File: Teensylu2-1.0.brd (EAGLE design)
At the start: 101.6 x 76.2 mm, 114 parts, among them J1 M02POLAR, J10 HOTEND-2, J11 M02POLAR, J12 M02POLAR, J13 M02POLAR, J2 MICROSD, J3 USB-MICRO-PTH, J4 M02POLAR, J5 4P-TERM-BLOCK284391-4, J6 39-29-3066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

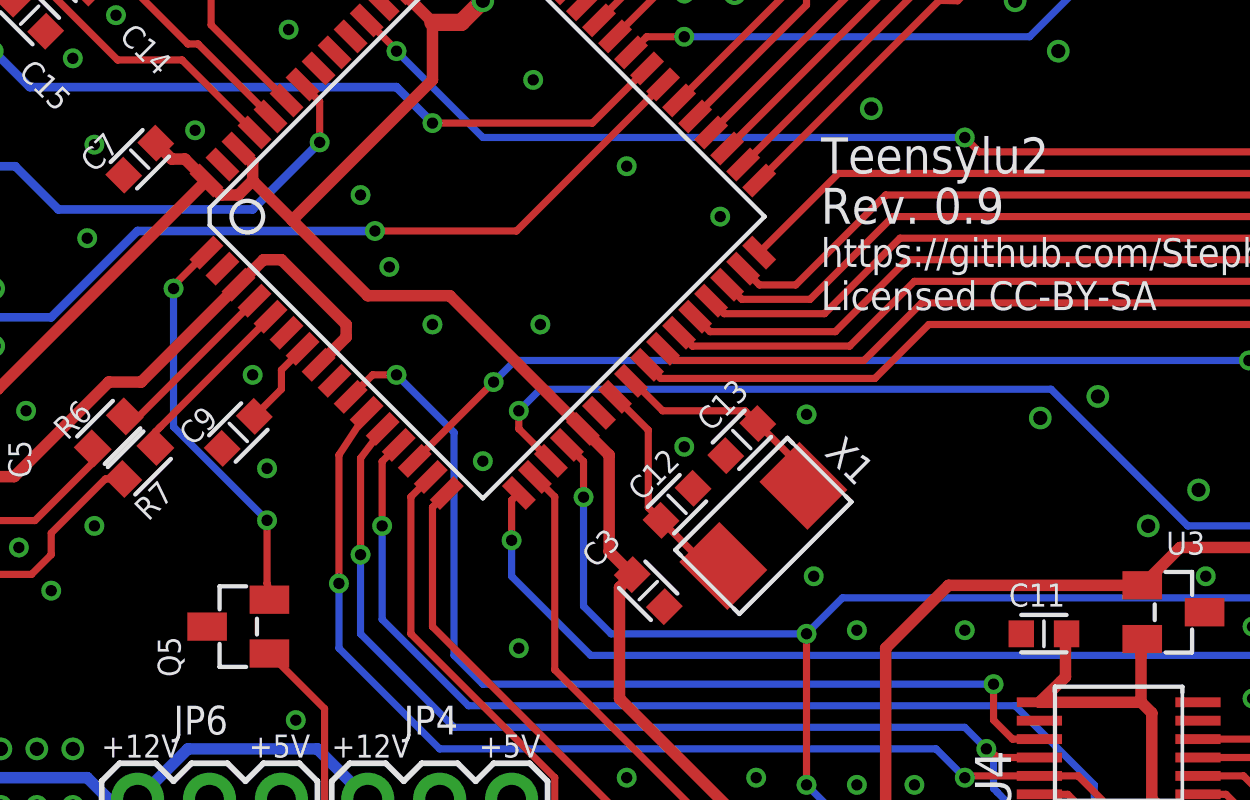
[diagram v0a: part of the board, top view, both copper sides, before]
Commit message: Fixed Z Endstop
Collector and Emitter were swapped.
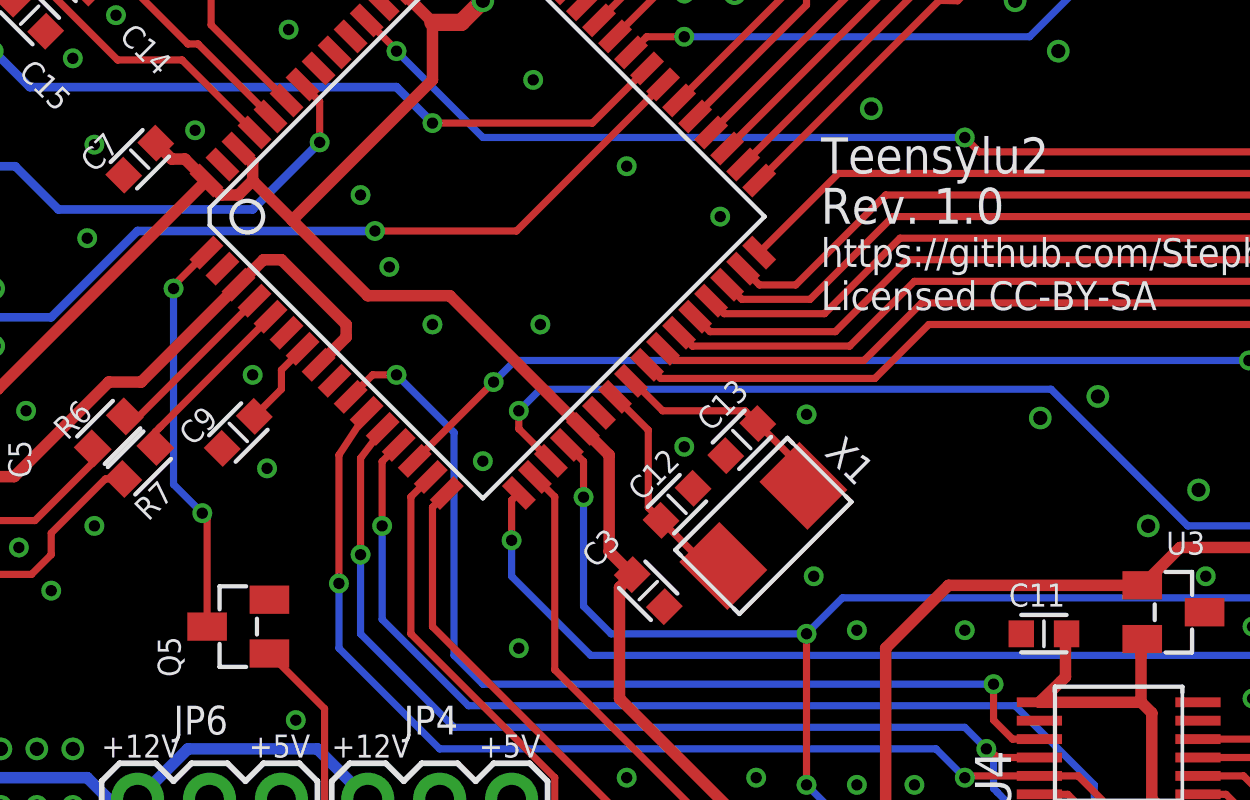
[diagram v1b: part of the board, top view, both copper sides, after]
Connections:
- net GND: now also Q5.2; no longer Q5.3
- net Z-STOP: now also Q5.3; no longer Q5.2
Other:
- board text added: "Rev. 1.0"
- board text removed: "Rev. 0.9"
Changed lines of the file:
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@@
 <text x="48.26" y="10.922" size="0.8128" layer="121" font="vector" ratio="15" rot="R180">+12V</text>
 <text x="62.738" y="30.734" size="1.27" layer="121" font="vector" ratio="15">Teensylu2</text>
-<text x="62.738" y="28.956" size="1.27" layer="121" font="vector" ratio="15">Rev. 0.9</text>
+<text x="62.738" y="28.956" size="1.27" layer="121" font="vector" ratio="15">Rev. 1.0</text>
 <text x="62.738" y="27.432" size="1.016" layer="121" font="vector" ratio="15">https://github.com/StephS/Teensylu2</text>
 <text x="62.738" y="25.908" size="1.016" layer="121" font="vector" ratio="15">Licensed CC-BY-SA</text>
@@
 <via x="16.764" y="54.864" extent="1-16" drill="0.4"/>
 <via x="86.106" y="56.388" extent="1-16" drill="0.4"/>
-<contactref element="Q5" pad="3"/>
 <via x="34.544" y="54.864" extent="1-16" drill="0.4"/>
 <via x="52.324" y="54.864" extent="1-16" drill="0.4"/>
 <via x="70.104" y="54.864" extent="1-16" drill="0.4"/>
 <via x="87.884" y="54.864" extent="1-16" drill="0.4"/>
+<contactref element="Q5" pad="2"/>
 <wire x1="97.282" y1="46.012" x2="93.726" y2="43.434" width="0" layer="19" extent="1-1"/>
 </signal>
@@
 </signal>
 <signal name="Z-STOP">
-<wire x1="43.18" y1="18.4843125" x2="43.18" y2="16.256" width="0.254" layer="1"/>
-<contactref element="Q5" pad="2"/>
-<wire x1="43.18" y1="16.256" x2="43.368" y2="15.682" width="0.254" layer="1"/>
-<wire x1="43.368" y1="15.682" x2="43.264" y2="15.682" width="0.254" layer="1"/>
 <contactref element="U5" pad="1"/>
 <wire x1="41.041925" y1="27.93720625" x2="39.878" y2="26.77328125" width="0.254" layer="1"/>
 <wire x1="39.878" y1="26.77328125" x2="39.878" y2="26.67" width="0.254" layer="1"/>
 <via x="39.878" y="26.67" extent="1-16" drill="0.4"/>
-<wire x1="39.878" y1="26.67" x2="39.878" y2="21.7863125" width="0.254" layer="16"/>
-<wire x1="39.878" y1="21.7863125" x2="43.18" y2="18.4843125" width="0.254" layer="16"/>
-<via x="43.18" y="18.4843125" extent="1-16" drill="0.4"/>
+<wire x1="39.878" y1="26.67" x2="39.878" y2="19.7543125" width="0.254" layer="16"/>
+<wire x1="39.878" y1="19.7543125" x2="40.894" y2="18.7383125" width="0.254" layer="16"/>
+<via x="40.894" y="18.7383125" extent="1-16" drill="0.4"/>
+<contactref element="Q5" pad="3"/>
+<wire x1="40.894" y1="18.7383125" x2="41.064" y2="18.5683125" width="0.254" layer="1"/>
+<wire x1="41.064" y1="18.5683125" x2="41.064" y2="14.732" width="0.254" layer="1"/>
 </signal>
 <signal name="X-STEP">
